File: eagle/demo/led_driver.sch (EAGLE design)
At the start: 13 parts, among them T101 BC548C, X1 CLAMP_1X2-T-2.5MM, X301 MALE_2X1-T-VERTICAL, X302 CLAMP_1X2-T-2.5MM

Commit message: kbd module
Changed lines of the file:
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@@
 <attribute name="FUNCTION" value="PWR IN"/>
 </part>
+<part name="FRAME_DEVELOPMENT2" library="be_frame" deviceset="A4_LANDSCAPE_DEVELOPMENT" device=""/>
 </parts>
 <sheets>
@@
 </instance>
 <instance part="GND1" gate="1" x="147.32" y="58.42"/>
-<instance part="GND4" gate="1" x="147.32" y="99.06"/>
-<instance part="FD301" gate="FD" x="27.94" y="30.48"/>
-<instance part="FD302" gate="FD" x="27.94" y="20.32"/>
-<instance part="H301" gate="G$1" x="53.34" y="30.48"/>
-<instance part="H302" gate="G$1" x="53.34" y="20.32"/>
-<instance part="X1" gate="G$1" x="137.16" y="106.68" rot="R180">
-<attribute name="FUNCTION" x="144.78" y="114.3" size="2.54" layer="96" font="fixed" rot="R180"/>
-</instance>
 </instances>
 <busses>
@@
 <pinref part="GND1" gate="1" pin="GND"/>
 </segment>
-<segment>
-<pinref part="X1" gate="G$1" pin="1"/>
-<pinref part="GND4" gate="1" pin="GND"/>
-<wire x1="139.7" y1="104.14" x2="147.32" y2="104.14" width="0.1524" layer="91"/>
-<wire x1="147.32" y1="104.14" x2="147.32" y2="101.6" width="0.1524" layer="91"/>
-</segment>
 </net>
 <net name="FRONTEND_DRV_OUT" class="0">
@@
 <label x="219.075" y="66.675" size="1.27" layer="95" font="fixed"/>
 </segment>
+</net>
+</nets>
+</sheet>
+<sheet>
+<plain>
+</plain>
+<instances>
+<instance part="FRAME_DEVELOPMENT2" gate="G$1" x="0" y="0"/>
+<instance part="GND4" gate="1" x="167.64" y="50.8"/>
+<instance part="FD301" gate="FD" x="35.56" y="30.48"/>
+<instance part="FD302" gate="FD" x="35.56" y="20.32"/>
+<instance part="H301" gate="G$1" x="60.96" y="30.48"/>
+<instance part="H302" gate="G$1" x="60.96" y="20.32"/>
+<instance part="X1" gate="G$1" x="157.48" y="58.42" rot="R180">
+<attribute name="FUNCTION" x="165.1" y="66.04" size="2.54" layer="96" font="fixed" rot="R180"/>
+</instance>
+</instances>
+<busses>
+</busses>
+<nets>
+<net name="GND" class="0">
+<segment>
+<pinref part="X1" gate="G$1" pin="1"/>
+<pinref part="GND4" gate="1" pin="GND"/>
+<wire x1="160.02" y1="55.88" x2="167.64" y2="55.88" width="0.1524" layer="91"/>
+<wire x1="167.64" y1="55.88" x2="167.64" y2="53.34" width="0.1524" layer="91"/>
+</segment>
+</net>
+<net name="P5V" class="0">
 <segment>
 <pinref part="X1" gate="G$1" pin="2"/>
-<wire x1="139.7" y1="106.68" x2="154.94" y2="106.68" width="0.1524" layer="91"/>
-<label x="151.13" y="107.315" size="1.27" layer="95" font="fixed"/>
+<wire x1="160.02" y1="58.42" x2="175.26" y2="58.42" width="0.1524" layer="91"/>
+<label x="171.45" y="59.055" size="1.27" layer="95" font="fixed"/>
 </segment>
 </net>

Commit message: fixed led driver
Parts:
- removed N201: NET_CHANGER-S-0.15MM, be_con_jump:NET_CHANGER-S-0.15MM
- removed N202: NET_CHANGER-S-0.3MM, be_con_jump:NET_CHANGER-S-0.3MM
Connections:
- removed net BACKEND_DRV_IN: N201.2, X301.2
- removed net FRONTEND_DRV_OUT: N202.1, X302.2
- net DRV_IN: now also X301.2; no longer N201.1
- net DRV_OUT: now also X302.2; no longer N202.2
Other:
- note removed: "BACKEND"
- note removed: "FRONTEND"
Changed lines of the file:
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@@
 <part name="GND2" library="be_supply" deviceset="GND" device=""/>
 <part name="FRAME_DEVELOPMENT1" library="be_frame" deviceset="A4_LANDSCAPE_DEVELOPMENT" device=""/>
-<part name="FRAME_NET_CHANGERS1" library="be_frame" deviceset="A4_LANDSCAPE_NET_CHANGERS" device=""/>
-<part name="N201" library="be_con_jump" deviceset="NET_CHANGER" device="-S-0.15MM"/>
-<part name="N202" library="be_con_jump" deviceset="NET_CHANGER" device="-S-0.3MM"/>
-<part name="U$1" library="be_info" deviceset="ARROW_1" device=""/>
-<part name="U$2" library="be_info" deviceset="ARROW_1" device=""/>
-<part name="U$3" library="be_info" deviceset="ARROW_1" device=""/>
-<part name="U$4" library="be_info" deviceset="ARROW_1" device=""/>
 <part name="X302" library="be_con_jump" deviceset="CLAMP_1X2" device="-T-2.5MM">
 <attribute name="FUNCTION" value="LED DRV OUT"/>
@@
 <sheet>
 <plain>
-<text x="160.02" y="68.58" size="1.27" layer="97" font="fixed">BACKEND</text>
-<text x="160.02" y="50.8" size="1.27" layer="97" font="fixed">FRONTEND</text>
-</plain>
-<instances>
-<instance part="FRAME_NET_CHANGERS1" gate="G$1" x="0" y="0"/>
-<instance part="N201" gate="G$1" x="162.56" y="63.5" rot="MR0"/>
-<instance part="N202" gate="G$1" x="162.56" y="45.72" rot="MR0"/>
-<instance part="U$1" gate="G$1" x="149.86" y="63.5" rot="R180"/>
-<instance part="U$2" gate="G$1" x="172.72" y="63.5" rot="R180"/>
-<instance part="U$3" gate="G$1" x="172.72" y="45.72" rot="R180"/>
-<instance part="U$4" gate="G$1" x="149.86" y="45.72" rot="R180"/>
-</instances>
-<busses>
-</busses>
-<nets>
-<net name="DRV_IN" class="0">
-<segment>
-<wire x1="170.18" y1="63.5" x2="177.8" y2="63.5" width="0.1524" layer="91"/>
-<label x="177.8" y="63.5" size="1.27" layer="95" font="fixed" xref="yes"/>
-<pinref part="N201" gate="G$1" pin="1"/>
-</segment>
-</net>
-<net name="BACKEND_DRV_IN" class="0">
-<segment>
-<pinref part="N201" gate="G$1" pin="2"/>
-<wire x1="154.94" y1="63.5" x2="147.32" y2="63.5" width="0.1524" layer="91"/>
-<label x="147.32" y="63.5" size="1.27" layer="95" font="fixed" rot="R180" xref="yes"/>
-</segment>
-</net>
-<net name="FRONTEND_DRV_OUT" class="0">
-<segment>
-<wire x1="170.18" y1="45.72" x2="177.8" y2="45.72" width="0.1524" layer="91"/>
-<label x="177.8" y="45.72" size="1.27" layer="95" font="fixed" xref="yes"/>
-<pinref part="N202" gate="G$1" pin="1"/>
-</segment>
-</net>
-<net name="DRV_OUT" class="0">
-<segment>
-<pinref part="N202" gate="G$1" pin="2"/>
-<wire x1="154.94" y1="45.72" x2="147.32" y2="45.72" width="0.1524" layer="91"/>
-<label x="147.32" y="45.72" size="1.27" layer="95" font="fixed" rot="R180" xref="yes"/>
-</segment>
-</net>
-</nets>
-</sheet>
-<sheet>
-<plain>
 </plain>
 <instances>
@@
 </busses>
 <nets>
-<net name="BACKEND_DRV_IN" class="0">
-<segment>
-<pinref part="X301" gate="G$1" pin="2"/>
-<wire x1="142.24" y1="68.58" x2="149.86" y2="68.58" width="0.1524" layer="91"/>
-<label x="149.86" y="68.58" size="1.27" layer="95" font="fixed" xref="yes"/>
-</segment>
-</net>
 <net name="GND" class="0">
 <segment>
@@
 </segment>
 </net>
-<net name="FRONTEND_DRV_OUT" class="0">
+<net name="DRV_OUT" class="0">
 <segment>
 <pinref part="X302" gate="G$1" pin="2"/>
@@
 </segment>
 </net>
+<net name="DRV_IN" class="0">
+<segment>
+<pinref part="X301" gate="G$1" pin="2"/>
+<wire x1="142.24" y1="68.58" x2="149.86" y2="68.58" width="0.1524" layer="91"/>
+<label x="149.86" y="68.58" size="1.27" layer="95" font="fixed" xref="yes"/>
+</segment>
+</net>

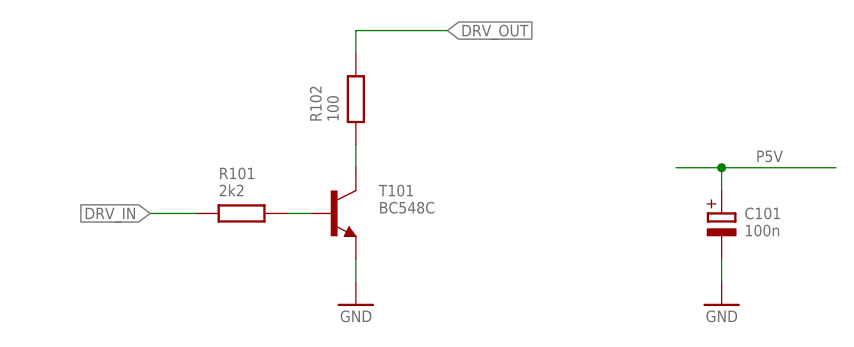
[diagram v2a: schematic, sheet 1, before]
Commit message: fixed prefixes
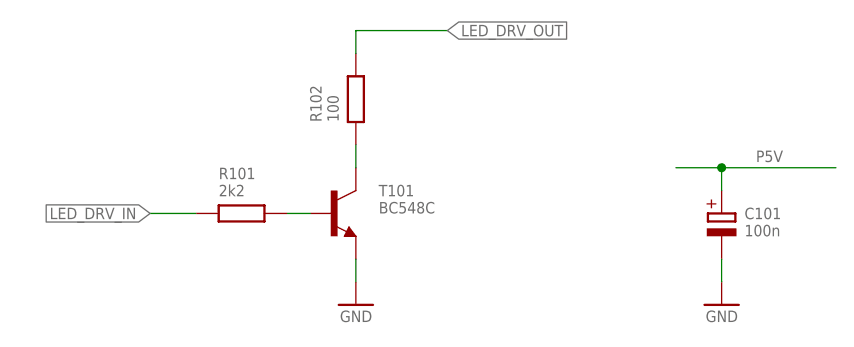
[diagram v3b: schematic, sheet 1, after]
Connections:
- net DRV_B renamed LED_DRV_B
- net DRV_C renamed LED_DRV_C
- net DRV_IN renamed LED_DRV_IN
- net DRV_OUT renamed LED_DRV_OUT
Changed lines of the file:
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@@
 </segment>
 </net>
-<net name="DRV_IN" class="0">
+<net name="LED_DRV_IN" class="0">
 <segment>
 <pinref part="R101" gate="G$1" pin="1"/>
@@
 </segment>
 </net>
-<net name="DRV_B" class="0">
+<net name="LED_DRV_B" class="0">
 <segment>
 <pinref part="R101" gate="G$1" pin="2"/>
@@
 </segment>
 </net>
-<net name="DRV_C" class="0">
+<net name="LED_DRV_C" class="0">
 <segment>
 <pinref part="T101" gate="G$1" pin="C"/>
@@
 </segment>
 </net>
-<net name="DRV_OUT" class="0">
+<net name="LED_DRV_OUT" class="0">
 <segment>
 <pinref part="R102" gate="G$1" pin="2"/>
@@
 </segment>
 </net>
-<net name="DRV_OUT" class="0">
+<net name="LED_DRV_OUT" class="0">
 <segment>
 <pinref part="X302" gate="G$1" pin="2"/>
@@
 </segment>
 </net>
-<net name="DRV_IN" class="0">
+<net name="LED_DRV_IN" class="0">
 <segment>
 <pinref part="X301" gate="G$1" pin="2"/>
